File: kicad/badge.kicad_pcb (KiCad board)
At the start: 2 copper layers, 76.2 x 101.6 mm, 29 parts, among them U1 ATtiny85-20P, U2 4021, U3 74HC595, U4 74HC595

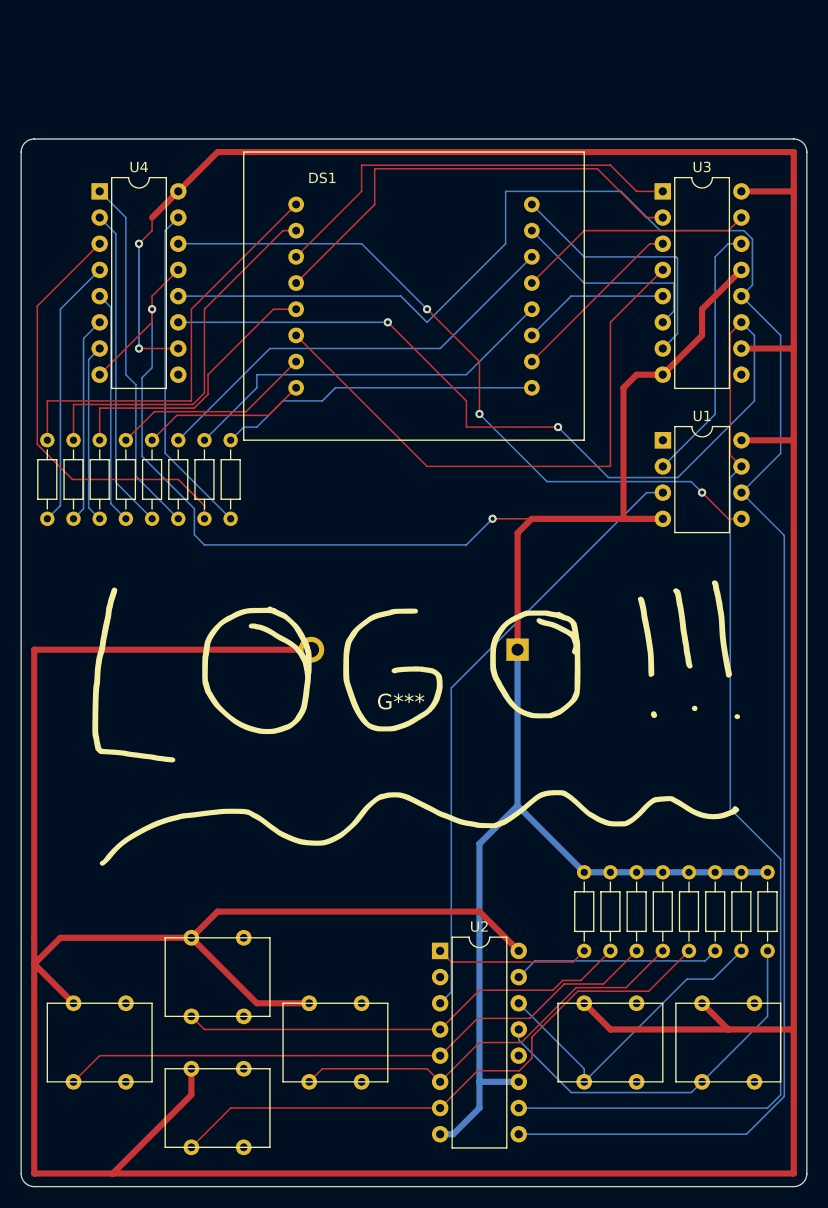
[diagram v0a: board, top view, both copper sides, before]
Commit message: Update badge with latest version
Signed-off-by: Josh Bressers <josh@bress.net>
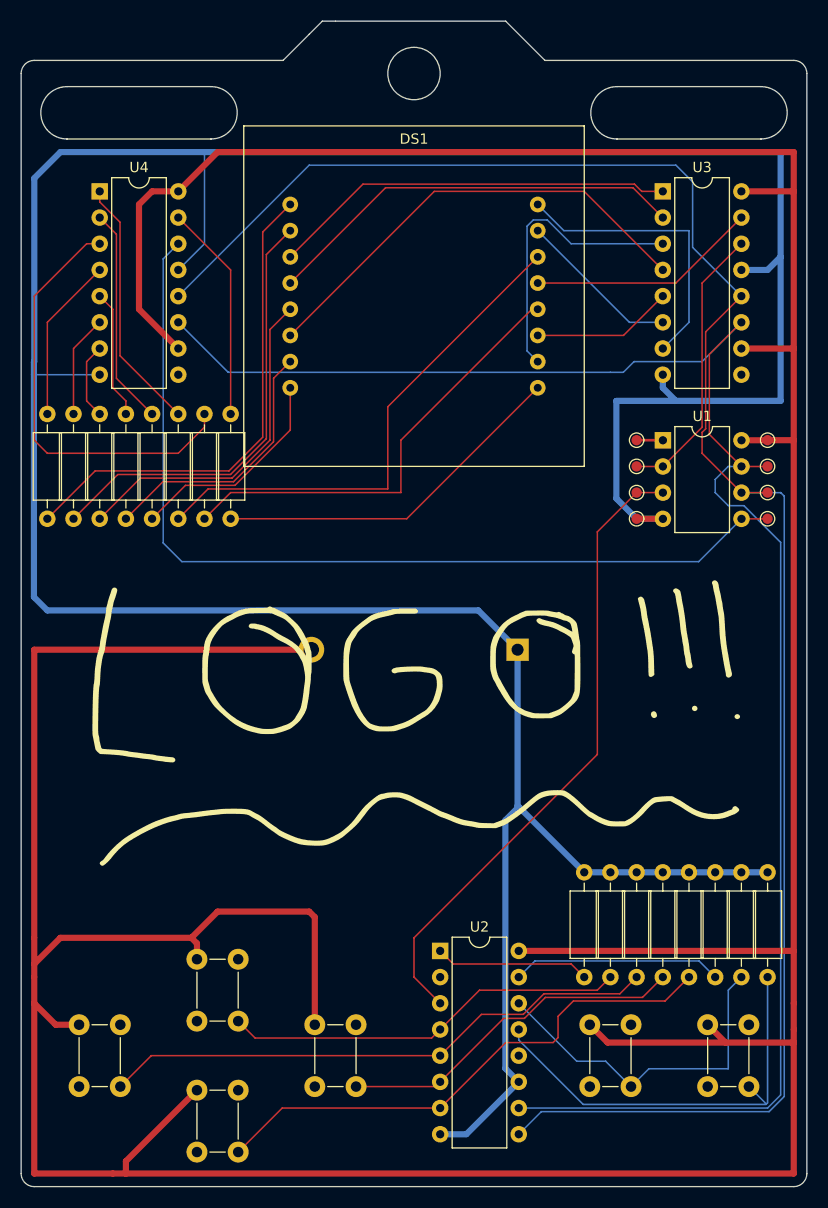
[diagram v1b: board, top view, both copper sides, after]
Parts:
- added TP1: TestPoint, TestPoint:TestPoint_Pad_D1.0mm, F.Cu at (212.1, 67.3)
- added TP2: TestPoint, TestPoint:TestPoint_Pad_D1.0mm, F.Cu at (212.1, 69.8)
- added TP3: TestPoint, TestPoint:TestPoint_Pad_D1.0mm, F.Cu at (212.1, 72.4)
- added TP4: TestPoint, TestPoint:TestPoint_Pad_D1.0mm, F.Cu at (212.1, 74.9)
- added TP5: TestPoint, TestPoint:TestPoint_Pad_D1.0mm, F.Cu at (224.8, 74.9)
- added TP6: TestPoint, TestPoint:TestPoint_Pad_D1.0mm, F.Cu at (224.8, 72.4)
- added TP7: TestPoint, TestPoint:TestPoint_Pad_D1.0mm, F.Cu at (224.8, 69.8)
- added TP8: TestPoint, TestPoint:TestPoint_Pad_D1.0mm, F.Cu at (224.8, 67.3)
- R1, R10, R11, R12, R13, R14, R15, R16, R2, R3, R4, R5, R6, R7, R8, R9: footprint Resistor_THT:R_Axial_DIN0204_L3.6mm_D1.6mm_P7.62mm_Horizontal -> Resistor_THT:R_Axial_DIN0207_L6.3mm_D2.5mm_P10.16mm_Horizontal
- moved R1 10.2 mm to (172.7, 64.8), turned to -90 degrees
- moved R2 10.2 mm to (167.6, 64.8), turned to -90 degrees
- moved R3 10.2 mm to (165.1, 64.8), turned to -90 degrees
- moved R4 10.2 mm to (170.2, 64.8), turned to -90 degrees
- moved R5 10.2 mm to (154.9, 64.8), turned to -90 degrees
- moved R6 10.2 mm to (162.6, 64.8), turned to -90 degrees
- moved R7 10.2 mm to (157.5, 64.8), turned to -90 degrees
- moved R8 10.2 mm to (160.0, 64.8), turned to -90 degrees
- moved R10 2.54 mm to (219.7, 119.4)
- moved R11 2.54 mm to (222.2, 119.4)
- moved R12 2.54 mm to (224.8, 119.4)
- moved R13 2.54 mm to (209.6, 119.4)
- moved R14 2.54 mm to (212.1, 119.4)
- moved R15 2.54 mm to (214.6, 119.4)
- moved R16 2.54 mm to (217.2, 119.4)
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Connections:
- S1 pad 3: Net-(U2-D0) -> unconnected-(S1-Pad3)
- S1 pad 4: unconnected-(S1-Pad4) -> Net-(U2-D0)
- S2 pad 3: Net-(U2-D1) -> unconnected-(S2-Pad3)
- S2 pad 4: unconnected-(S2-Pad4) -> Net-(U2-D1)
- S3 pad 3: Net-(U2-D2) -> unconnected-(S3-Pad3)
- S3 pad 4: unconnected-(S3-Pad4) -> Net-(U2-D2)
- S4 pad 3: Net-(U2-D3) -> unconnected-(S4-Pad3)
- S4 pad 4: unconnected-(S4-Pad4) -> Net-(U2-D3)
- S5 pad 3: Net-(U2-D4) -> unconnected-(S5-Pad3)
- S5 pad 4: unconnected-(S5-Pad4) -> Net-(U2-D4)
- S6 pad 3: Net-(U2-D5) -> unconnected-(S6-Pad3)
- S6 pad 4: unconnected-(S6-Pad4) -> Net-(U2-D5)
- U1 pad 1: unconnected-(U1-~{RESET}/PB5-Pad1) -> Net-(U1-~{RESET}/PB5)
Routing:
- net GND: track 209.8 -> 326.3 mm, vias 2 -> 0
- net Net-(U1-AREF/PB0): track 68.6 -> 90.7 mm, vias 3 -> 0
- net Net-(DS1-C5): track 56.9 -> 45.1 mm
- net Net-(U4-QA): track 32.4 -> 21.2 mm
- net Net-(DS1-C4): track 17.4 -> 27.9 mm
- net Net-(U4-QE): track 26.2 -> 16.1 mm
- net Net-(U4-QG): track 20.1 -> 9.94 mm
- net Net-(U4-QF): track 22.6 -> 12.5 mm
- net Net-(U4-QC): track 31.3 -> 21.2 mm
- net Net-(U4-QB): track 34.9 -> 24.7 mm
- net Net-(U4-QH): track 17.4 -> 7.40 mm
- net Net-(U1-PB2): track 179.1 -> 169.9 mm, vias 2 -> 0
- net Net-(DS1-R2): track 41.7 -> 50.0 mm
- net Net-(DS1-R5): track 41.0 -> 47.8 mm
- net Net-(DS1-R7): track 36.8 -> 43.1 mm
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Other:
- board size 76.2 x 101.6 mm -> 76.2 x 113 mm

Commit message: Update badge PCB
Signed-off-by: Josh Bressers <josh@bress.net>
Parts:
- TP1, TP2, TP3, TP4, TP5, TP6, TP7, TP8: footprint TestPoint:TestPoint_Pad_D1.0mm -> TestPoint:TestPoint_THTPad_D1.5mm_Drill0.7mm
- U1: value ATtiny85-20P -> ATtiny85
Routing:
- net Net-(U4-QD): track 41.8 -> 21.2 mm
- net Net-(DS1-C5): track 45.1 -> 53.2 mm
- net VCC: track 454.8 -> 447.2 mm
- net Net-(U1-PB2): track 169.9 -> 166.4 mm
- net Net-(U1-AREF/PB0): track 90.7 -> 94.1 mm
- net Net-(DS1-R2): track 50.0 -> 47.0 mm
- net Net-(U1-PB1): track 183.4 -> 180.6 mm
- net Net-(DS1-C3): track 41.2 -> 43.9 mm
- net GND: track 326.3 -> 328.8 mm
- net Net-(DS1-R1): track 35.0 -> 37.4 mm
- net Net-(U2-D5): track 33.8 -> 31.5 mm
- net Net-(DS1-C2): track 39.3 -> 40.9 mm
- net Net-(DS1-R4): track 43.7 -> 42.4 mm
- net Net-(U2-D4): track 42.4 -> 43.8 mm
- net Net-(U2-D3): track 39.2 -> 40.4 mm
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
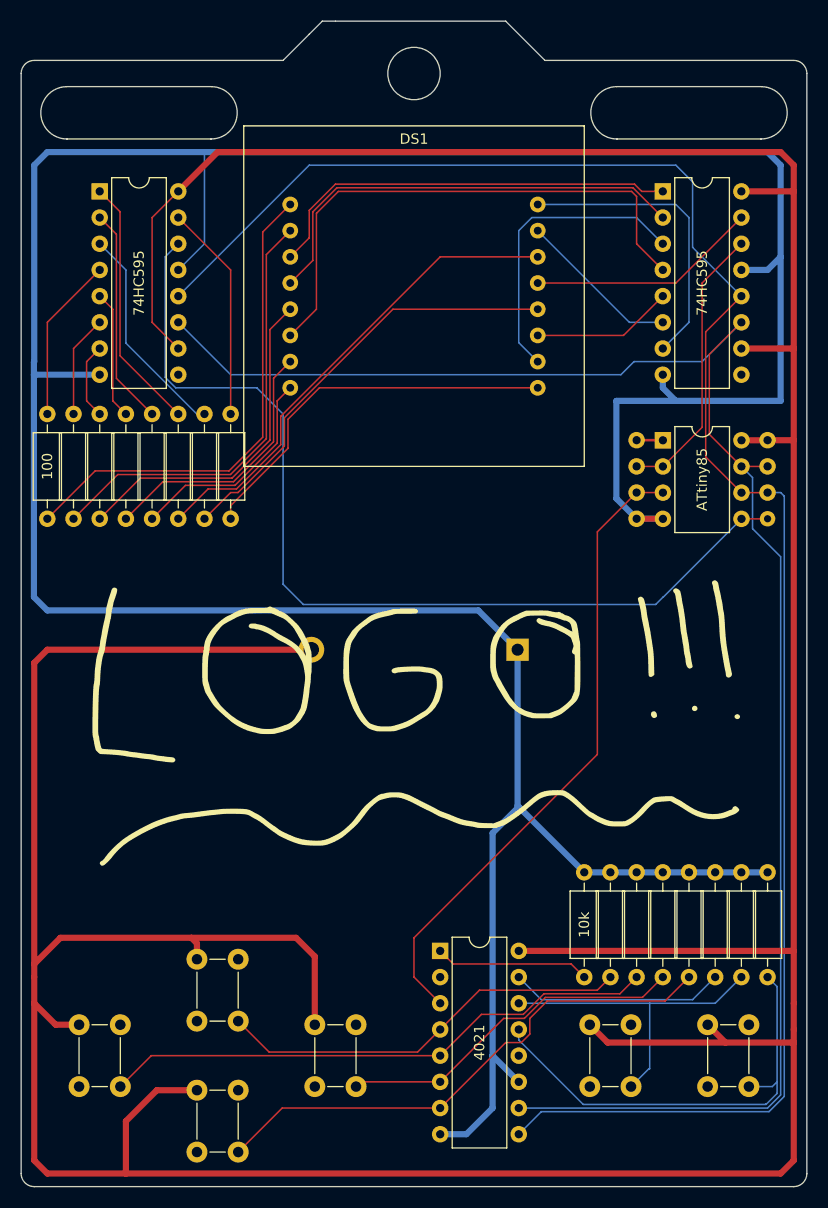
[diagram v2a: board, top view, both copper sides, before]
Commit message: Add changes to badge to match reality
Signed-off-by: Josh Bressers <josh@bress.net>
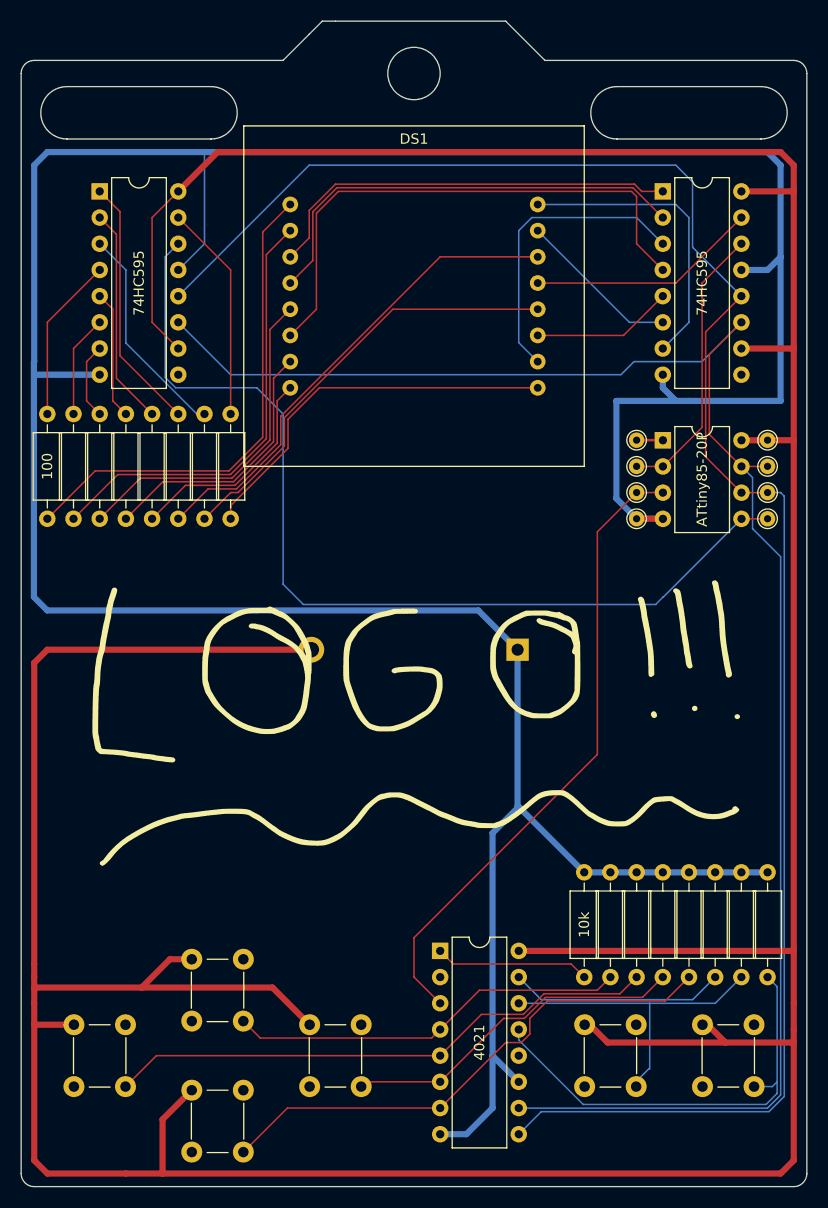
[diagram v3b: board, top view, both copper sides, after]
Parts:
- U1: value ATtiny85 -> ATtiny85-20P
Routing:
- net VCC: track 447.2 -> 438.2 mm
- net Net-(U2-D3): track 40.4 -> 38.7 mm
- net Net-(U2-D2): track 54.5 -> 54.0 mm
- net Net-(U2-D0): track 51.6 -> 51.1 mm
